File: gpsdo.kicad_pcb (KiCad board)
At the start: 2 copper layers, 124 parts, among them U1 LM2937IMP-5.0, U10 MC12080, U11 MSA-0385, U12 MSA-0385, U13 MSA-0385, U14 MSA-0385, U15 MSA-0385, U16 MSA-0385, U17 MSA-0385, U18 MSA-0385, U19 MSA-0385, U2 LM2937IMP-8.0, U20 MSA-0385, U21 MSA-0385, U3 SN74HC244, U4 TPS79333-EP, U5 ADP7142ARDZ-5.0-R7, U6 DAC8571IDGKR, U7 LEA-M8F, U8 CVSS-945, U9 SN74HC244

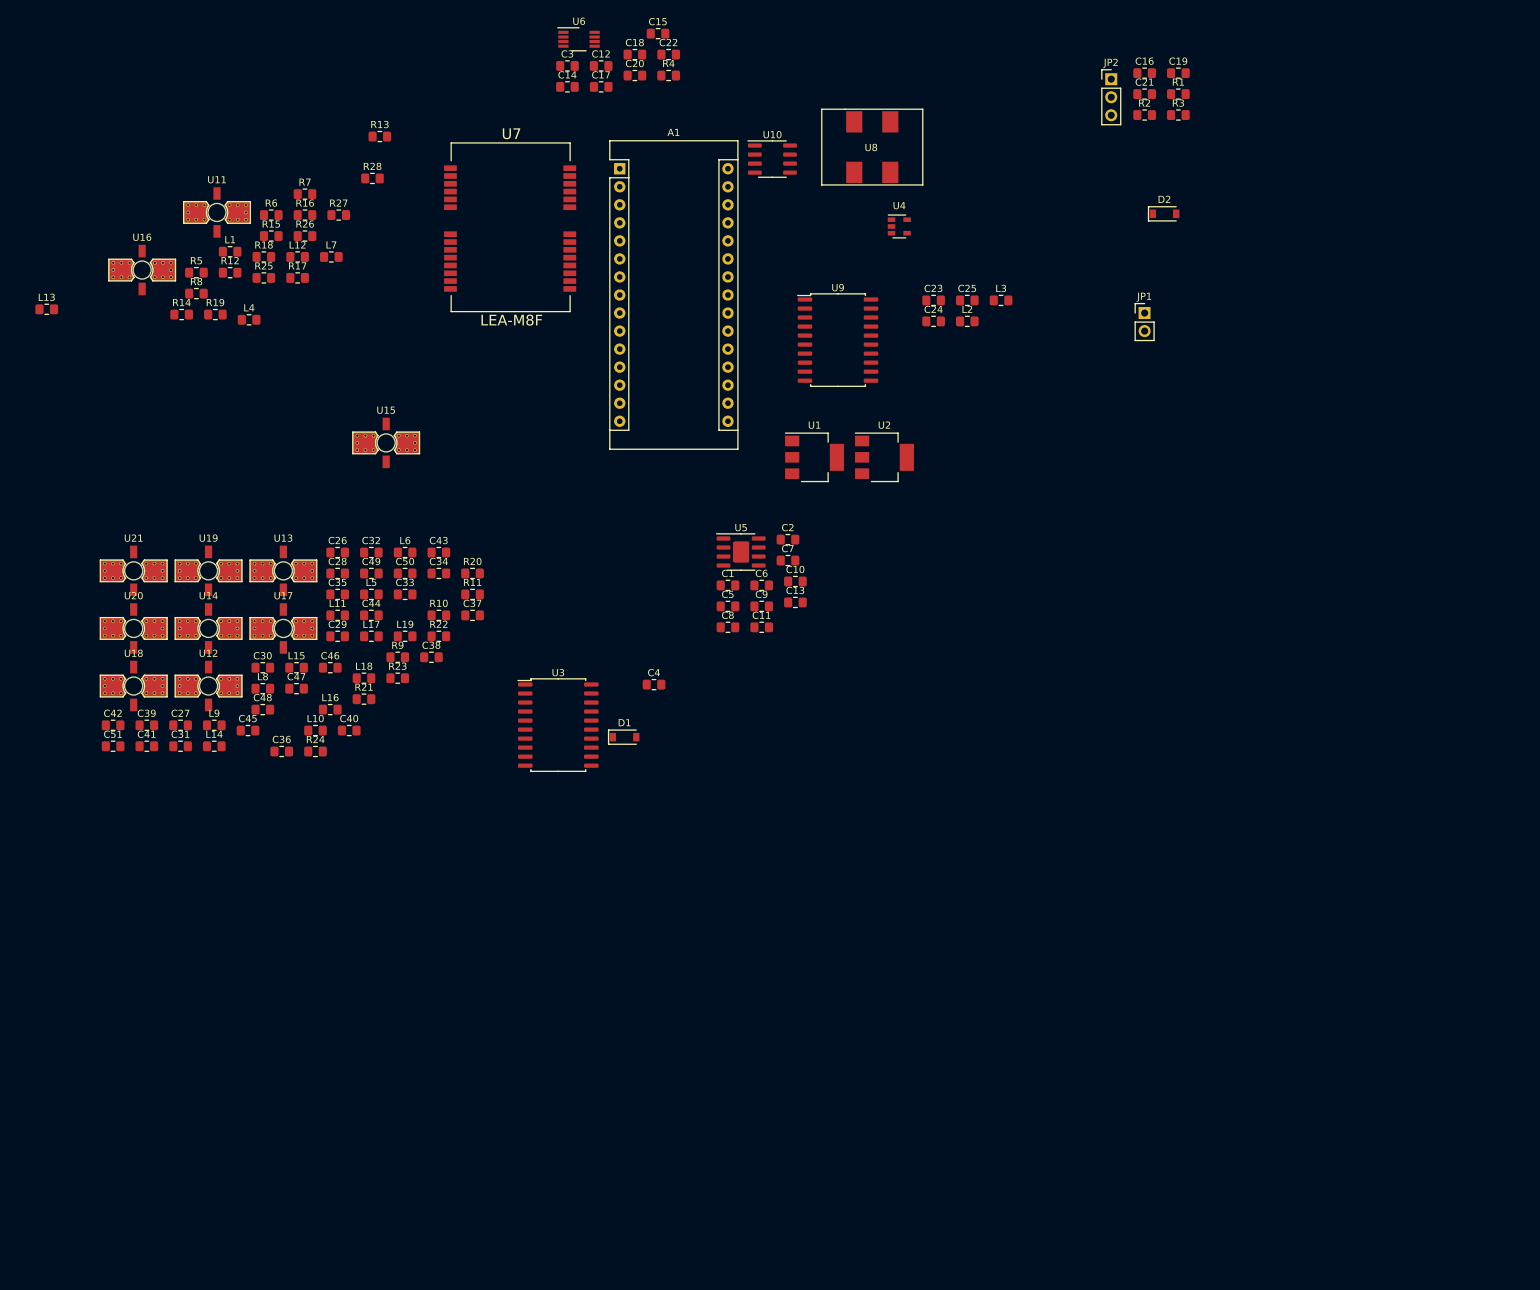
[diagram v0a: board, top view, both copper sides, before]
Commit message: Implemented fixes following Frederic's review
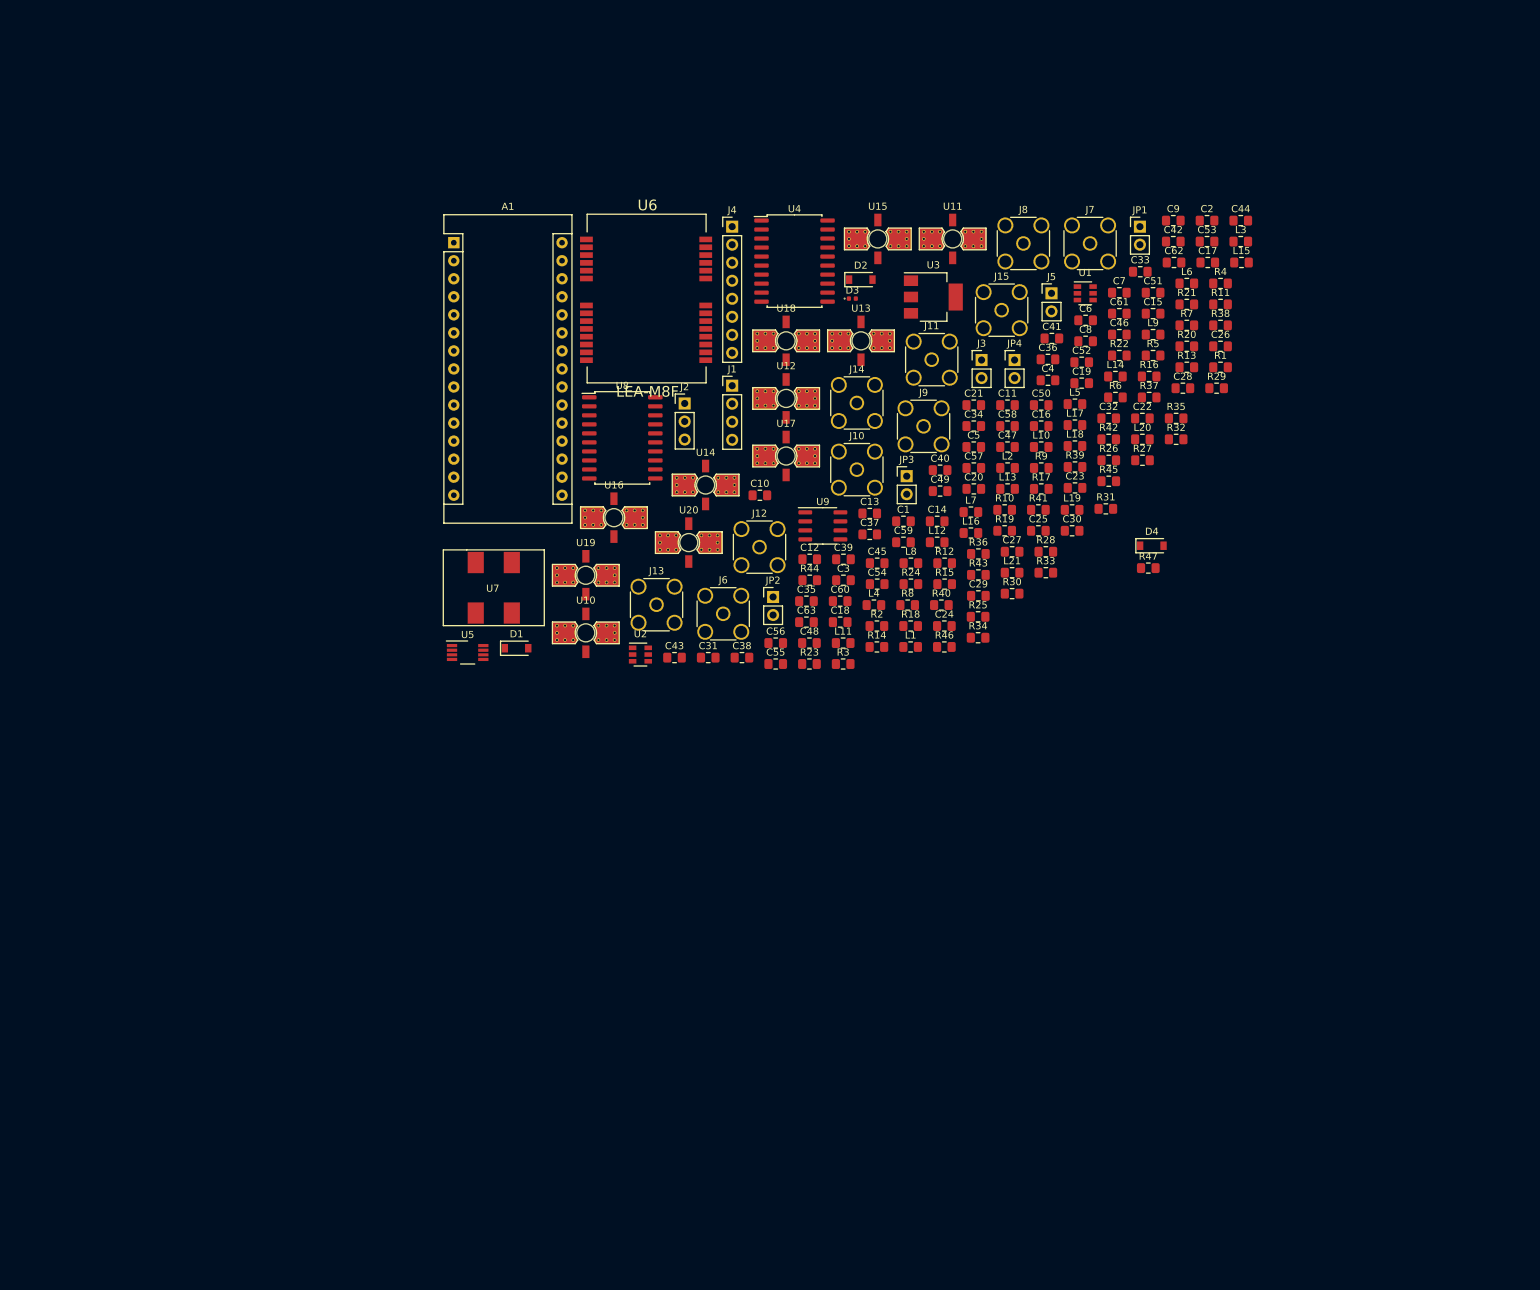
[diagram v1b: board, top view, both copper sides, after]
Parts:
- removed U21: MSA-0385, yo6ssw:PL262
- added C52: 0.1uF, Capacitor_SMD:C_0805_2012Metric_Pad1.15x1.40mm_HandSolder, F.Cu at (166.4, 73.0)
- added C53: 0.1uF, Capacitor_SMD:C_0805_2012Metric_Pad1.15x1.40mm_HandSolder, F.Cu at (184.0, 56.0)
- added C54: 0.1uF, Capacitor_SMD:C_0805_2012Metric_Pad1.15x1.40mm_HandSolder, F.Cu at (137.6, 104.2)
- added C55: 0.1uF, Capacitor_SMD:C_0805_2012Metric_Pad1.15x1.40mm_HandSolder, F.Cu at (123.3, 115.5)
- added C56: 0.1uF, Capacitor_SMD:C_0805_2012Metric_Pad1.15x1.40mm_HandSolder, F.Cu at (123.3, 112.5)
- added C57: 0.1uF, Capacitor_SMD:C_0805_2012Metric_Pad1.15x1.40mm_HandSolder, F.Cu at (151.2, 87.9)
- added C58: 0.1uF, Capacitor_SMD:C_0805_2012Metric_Pad1.15x1.40mm_HandSolder, F.Cu at (155.9, 82.0)
- added C59: 0.1uF, Capacitor_SMD:C_0805_2012Metric_Pad1.15x1.40mm_HandSolder, F.Cu at (141.3, 98.3)
- added C60: 0.1uF, Capacitor_SMD:C_0805_2012Metric_Pad1.15x1.40mm_HandSolder, F.Cu at (132.4, 106.6)
- added C61: 0.1uF, Capacitor_SMD:C_0805_2012Metric_Pad1.15x1.40mm_HandSolder, F.Cu at (171.7, 66.1)
- added C62: 0.1uF, Capacitor_SMD:C_0805_2012Metric_Pad1.15x1.40mm_HandSolder, F.Cu at (179.4, 58.9)
- added C63: 0.1uF, Capacitor_SMD:C_0805_2012Metric_Pad1.15x1.40mm_HandSolder, F.Cu at (127.6, 109.6)
- added D3: ESD9R3.3ST5G, Diode_SMD:D_0402_1005Metric, F.Cu at (134.1, 64.0)
- added D4: 1N4148W, Diode_SMD:D_SOD-123, F.Cu at (176.3, 98.8)
- added J1: OLED, Connector_PinHeader_2.54mm:PinHeader_1x04_P2.54mm_Vertical, F.Cu at (117.2, 76.3)
- added J10: 10MHZ_OUT, Connector_Coaxial:SMA_Amphenol_132134_Vertical, F.Cu at (134.7, 88.1)
- added J11: 100MHZ_OUT, Connector_Coaxial:SMA_Amphenol_132134_Vertical, F.Cu at (145.3, 72.6)
- added J12: 10MHZ_OUT, Connector_Coaxial:SMA_Amphenol_132134_Vertical, F.Cu at (121.0, 99.0)
- added J13: 10MHZ_OUT, Connector_Coaxial:SMA_Amphenol_132134_Vertical, F.Cu at (106.5, 107.1)
- added J14: 10MHZ_OUT, Connector_Coaxial:SMA_Amphenol_132134_Vertical, F.Cu at (134.7, 78.7)
- added J15: 10MHZ_OUT, Connector_Coaxial:SMA_Amphenol_132134_Vertical, F.Cu at (155.1, 65.6)
- added J2: ARDUINO_UART, Connector_PinHeader_2.54mm:PinHeader_1x03_P2.54mm_Vertical, F.Cu at (110.5, 78.8)
- added J3: VOLTMETER, Connector_PinHeader_2.54mm:PinHeader_1x02_P2.54mm_Vertical, F.Cu at (152.3, 72.7)
- added J4: ARDUINO_EXTRA_PINS, Connector_PinHeader_2.54mm:PinHeader_1x08_P2.54mm_Vertical, F.Cu at (117.2, 53.9)
- added J5: POWER_IN, Connector_PinHeader_2.54mm:PinHeader_1x02_P2.54mm_Vertical, F.Cu at (162.1, 63.3)
- added J6: GPS_ANT, Connector_Coaxial:SMA_Amphenol_132134_Vertical, F.Cu at (115.9, 108.4)
- added J7: 10MHZ_OUT, Connector_Coaxial:SMA_Amphenol_132134_Vertical, F.Cu at (167.6, 56.2)
- added J8: 10MHZ_OUT, Connector_Coaxial:SMA_Amphenol_132134_Vertical, F.Cu at (158.2, 56.2)
- added J9: 10MHZ_OUT, Connector_Coaxial:SMA_Amphenol_132134_Vertical, F.Cu at (144.1, 82.0)
- added JP3: JP_BUF_1_OUT, Connector_PinHeader_2.54mm:PinHeader_1x02_P2.54mm_Vertical, F.Cu at (141.8, 89.0)
- added JP4: JP_BUF_2_OUT, Connector_PinHeader_2.54mm:PinHeader_1x02_P2.54mm_Vertical, F.Cu at (156.9, 72.7)
- added L20: 1uH, Inductor_SMD:L_0805_2012Metric_Pad1.15x1.40mm_HandSolder, F.Cu at (174.9, 83.8)
- added L21: 1uH, Inductor_SMD:L_0805_2012Metric_Pad1.15x1.40mm_HandSolder, F.Cu at (156.6, 102.6)
- added R29: 86.6Ω 1%, Resistor_SMD:R_0805_2012Metric_Pad1.15x1.40mm_HandSolder, F.Cu at (185.4, 76.6)
- added R30: 86.6Ω 1%, Resistor_SMD:R_0805_2012Metric_Pad1.15x1.40mm_HandSolder, F.Cu at (156.6, 105.6)
- added R31: 86.6Ω 1%, Resistor_SMD:R_0805_2012Metric_Pad1.15x1.40mm_HandSolder, F.Cu at (169.8, 93.6)
- added R32: 30Ω, Resistor_SMD:R_0805_2012Metric_Pad1.15x1.40mm_HandSolder, F.Cu at (179.7, 83.8)
- added R33: 30Ω, Resistor_SMD:R_0805_2012Metric_Pad1.15x1.40mm_HandSolder, F.Cu at (161.3, 102.6)
- added R34: 30Ω, Resistor_SMD:R_0805_2012Metric_Pad1.15x1.40mm_HandSolder, F.Cu at (151.8, 111.8)
- added R35: 30Ω, Resistor_SMD:R_0805_2012Metric_Pad1.15x1.40mm_HandSolder, F.Cu at (179.7, 80.9)
- added R36: 30Ω, Resistor_SMD:R_0805_2012Metric_Pad1.15x1.40mm_HandSolder, F.Cu at (151.8, 100.0)
- added R37: 30Ω, Resistor_SMD:R_0805_2012Metric_Pad1.15x1.40mm_HandSolder, F.Cu at (175.9, 77.9)
- added R38: 86.6Ω 1%, Resistor_SMD:R_0805_2012Metric_Pad1.15x1.40mm_HandSolder, F.Cu at (185.9, 67.8)
- added R39: 86.6Ω 1%, Resistor_SMD:R_0805_2012Metric_Pad1.15x1.40mm_HandSolder, F.Cu at (165.5, 87.7)
- added R40: 86.6Ω 1%, Resistor_SMD:R_0805_2012Metric_Pad1.15x1.40mm_HandSolder, F.Cu at (146.6, 107.2)
- added R41: 86.6Ω 1%, Resistor_SMD:R_0805_2012Metric_Pad1.15x1.40mm_HandSolder, F.Cu at (160.3, 93.8)
- added R42: 86.6Ω 1%, Resistor_SMD:R_0805_2012Metric_Pad1.15x1.40mm_HandSolder, F.Cu at (170.2, 83.8)
- added R43: 30Ω, Resistor_SMD:R_0805_2012Metric_Pad1.15x1.40mm_HandSolder, F.Cu at (151.8, 102.9)
- added R44: 30Ω, Resistor_SMD:R_0805_2012Metric_Pad1.15x1.40mm_HandSolder, F.Cu at (128.1, 103.7)
- added R45: 30Ω, Resistor_SMD:R_0805_2012Metric_Pad1.15x1.40mm_HandSolder, F.Cu at (170.2, 89.7)
- added R46: 30Ω, Resistor_SMD:R_0805_2012Metric_Pad1.15x1.40mm_HandSolder, F.Cu at (147.1, 113.1)
- added R47: 100KΩ, Resistor_SMD:R_0805_2012Metric_Pad1.15x1.40mm_HandSolder, F.Cu at (175.8, 102.0)
- C10: value 3.3uF/6.3V -> 15pF
- C11: value 0.01uF -> 0.1uF
- C12, C19, C2, C20, C3, C4: value 0.1uF -> 1uF
- C13: value 2.2uF/10V -> 1uF
- C14: value 0.1uF -> 2.2uF/6.3V
- C15: value 0.1uF -> 2.2uF/10V
- C17, C18: value 1nF -> 0.1uF
- C22: value CL -> 0.1uF
- C23, C25, C39: value 10p -> 0.1uF
- C24: value 100p -> 0.1uF
- C27, C28: value 0.1uF -> 1nF
- C29: value 0.1uF -> 100pF
- C31, C35, C36: value 0.1uF -> 443.2pF
- C33: value 10p -> CL
- C34: value 100p -> 519.8pF
- C44, C50, C51: value 0.1uF -> 44.32pF
- C45: value 0.1uF -> 51.98pF
- C5: value 10uF/10V/ESR=2 -> 0.1uF
- C6: value 10uF/16V/ESR=2 -> 0.1uF
- C7: value 0.1uF -> 0.01uF
- C8: value 2.2uF/20V -> 0.01uF
- C9: value 0.01uF -> 15pF
- D2: value ANT_PROTECTION -> 1N4148W
- JP1: value JMP_DAC_VOLTAGE -> JP_BUF_1_IN
- JP2: value GPS_ANT_TYPE -> JP_BUF_2_IN; footprint Connector_PinHeader_2.54mm:PinHeader_1x03_P2.54mm_Vertical -> Connector_PinHeader_2.54mm:PinHeader_1x02_P2.54mm_Vertical
- L1, L2, L3, L4: value 2.2uH -> 10uH
- L11, L14: value 2.2uH -> 1uH
- L13, L8: value 1uH -> 139.1nH
- L16: value 1uH -> 63.42nH
- L5, L6: value 2.2uH -> 1.391uH
- L7: value 1uH -> 0.634uH
- R1: value 16.7Ω -> 100KΩ
- R10, R9: value 86.6Ω 1% -> 30KΩ
- R11, R12: value 86.6Ω 1% -> TBD
- R13: value 86.6Ω 1% -> 10K
- R14: value 30Ω -> 10K
- R15, R16: value 30Ω -> 100KΩ
- R17: value 30Ω -> 16.7Ω
- R18, R19, R25: value 30Ω -> 16.7Ω 1%
- R2: value 16.7Ω 1% -> 100KΩ
- R20: value 86.6Ω 1% -> 820Ω
- R21: value 86.6Ω 1% -> 220Ω
- R22: value 86.6Ω 1% -> 68Ω
- R23: value 86.6Ω 1% -> 16.7Ω
- R24: value 86.6Ω 1% -> 16.7Ω 1%
- R26, R27, R28: value 30Ω -> 86.6Ω 1%
- R3: value 16.7Ω 1% -> 18KΩ
- R4: value RL -> 33KΩ
- R5: value 16.7Ω -> 1.3KΩ
- R6: value 16.7Ω 1% -> 240Ω
- R7: value 16.7Ω 1% -> 56KΩ
- R8: value 86.6Ω 1% -> 93KΩ
- U1: value LM2937IMP-5.0 -> TPS79301-EP; footprint Package_TO_SOT_SMD:SOT-223-3_TabPin2 -> Package_TO_SOT_SMD:SOT-23-6
- U10: value MC12080 -> MSA-0385; footprint Package_SO:SOIC-8_3.9x4.9mm_P1.27mm -> yo6ssw:PL262
- U2: value LM2937IMP-8.0 -> TPS79301-EP; footprint Package_TO_SOT_SMD:SOT-223-3_TabPin2 -> Package_TO_SOT_SMD:SOT-23-6
- U3: value SN74HC244 -> LM317DCYR; footprint Package_SO:SOIC-20W_7.5x12.8mm_P1.27mm -> Package_TO_SOT_SMD:SOT-223
- U4: value TPS79333-EP -> SN74HC244; footprint Package_TO_SOT_SMD:SOT-23-5 -> Package_SO:SOIC-20W_7.5x12.8mm_P1.27mm
- U5: value ADP7142ARDZ-5.0-R7 -> DAC8571IDGKR; footprint Package_SO:SOIC-8-1EP_3.9x4.9mm_P1.27mm_EP2.29x3mm -> Package_SO:VSSOP-8_3.0x3.0mm_P0.65mm
- U6: value DAC8571IDGKR -> LEA-M8F; footprint Package_SO:VSSOP-8_3.0x3.0mm_P0.65mm -> yo6ssw:LEA-8MF
- U7: value LEA-M8F -> CVSS-945; footprint yo6ssw:LEA-8MF -> yo6ssw:CVSS-945
- U8: value CVSS-945 -> SN74HC244; footprint yo6ssw:CVSS-945 -> Package_SO:SOIC-20W_7.5x12.8mm_P1.27mm
- U9: value SN74HC244 -> MC12080; footprint Package_SO:SOIC-20W_7.5x12.8mm_P1.27mm -> Package_SO:SOIC-8_3.9x4.9mm_P1.27mm
- moved C42 164.1 mm to (179.3, 56.0)
- moved C51 159.8 mm to (176.4, 63.2)
- moved L15 144.8 mm to (188.9, 58.9)
- moved L9 143.2 mm to (176.4, 69.1)
- moved C41 139.8 mm to (162.2, 69.6)
- moved L13 137.6 mm to (156.0, 90.8)
- moved L14 137.2 mm to (171.1, 75.0)
- moved R5 135.2 mm to (176.4, 72.0)
- moved C44 134.5 mm to (188.8, 53.0)
- moved R21 128.5 mm to (181.2, 64.8)
- moved C26 127.7 mm to (185.9, 70.7)
- moved R7 125.5 mm to (181.2, 67.8)
- moved C28 121.9 mm to (180.6, 76.6)
- moved R6 121.6 mm to (171.1, 77.9)
- moved C36 121.2 mm to (161.6, 72.6)
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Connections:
- A1 pad 1: (no net) -> ARDUINO_UART_TX
- A1 pad 10: (no net) -> ARDUINO_D7
- A1 pad 12: (no net) -> VOLTMETER
- A1 pad 13: ARDUINO_RX -> A2G_RX
- A1 pad 14: ARDUINO_TX -> A2G_TX
- A1 pad 2: (no net) -> ARDUINO_UART_RX
- A1 pad 23: (no net) -> ARDUINO_SDA
- A1 pad 24: (no net) -> ARDUINO_SCL
- A1 pad 27: (no net) -> ARDUINO_5V
- A1 pad 30: V_ARDUINO -> Net-(A1-Pad30)
- A1 pad 5: (no net) -> ARDUINO_D2
- A1 pad 6: (no net) -> ARDUINO_D3
- A1 pad 7: (no net) -> ARDUINO_D4
- A1 pad 8: (no net) -> ARDUINO_D5
- A1 pad 9: (no net) -> ARDUINO_D6
- C1 pad 1: GND -> 10MHZ
- C1 pad 2: Vin -> Net-(C1-Pad2)
- C10 pad 1: V_GPS -> V_VCXO
- C10 pad 2: GND -> Net-(C10-Pad2)
- C11 pad 2: Net-(C11-Pad2) -> V_GPS
- C12 pad 2: V_GPS -> Net-(C12-Pad2)
- C13 pad 1: V_VCXO -> GND
- C13 pad 2: GND -> V_MMIC
- C14 pad 2: Net-(C14-Pad2) -> V_GPS
- C16 pad 1: 100MHZ_IN -> GND
- C16 pad 2: Net-(C16-Pad2) -> V_GPS
- C17 pad 1: Net-(C17-Pad1) -> GND
- C19 pad 2: V_ARDUINO -> Net-(C19-Pad2)
- C2 pad 2: Vin -> V_IN
- C20 pad 2: V_ARDUINO -> Net-(C20-Pad2)
- C21 pad 1: Net-(C21-Pad1) -> 10MHZ
- C21 pad 2: 100MHZ_IN -> Net-(C21-Pad2)
- C22 pad 2: 10MHZ_IN -> V_VCXO
- C24 pad 1: Net-(C24-Pad1) -> 100MHZ_FILTER
- C24 pad 2: GND -> Net-(C24-Pad2)
- C25 pad 1: Net-(C25-Pad1) -> GND
- C25 pad 2: GND -> V_VCXO
- C26 pad 1: Net-(C26-Pad1) -> GND
- C27 pad 1: /A1_IN -> Net-(C27-Pad1)
- C28 pad 1: /A3_IN -> GND
- C29 pad 1: /A5_IN -> GND
- C29 pad 2: Net-(C29-Pad2) -> V_VCXO
- C3 pad 2: V_ARDUINO -> V_IN
- C30 pad 1: /A7_IN -> GND
- C30 pad 2: Net-(C30-Pad2) -> V_VCXO
- C31 pad 1: Net-(C31-Pad1) -> GND
- C31 pad 2: Net-(C31-Pad2) -> 10MHZ_FILTER
- C33 pad 2: Net-(C33-Pad2) -> 10MHZ
- C35 pad 2: (no net) -> GND
- C36 pad 2: (no net) -> GND
- C37 pad 1: Net-(C37-Pad1) -> Net-(C36-Pad1)
- C37 pad 2: (no net) -> Net-(C37-Pad2)
- C38 pad 1: Net-(C38-Pad1) -> /A1_IN
- C38 pad 2: (no net) -> Net-(C38-Pad2)
- C39 pad 1: Net-(C39-Pad1) -> /A3_IN
- C39 pad 2: GND -> Net-(C39-Pad2)
- C4 pad 2: V_GPS -> V_IN
- C40 pad 1: Net-(C40-Pad1) -> /A5_IN
- C41 pad 1: Net-(C41-Pad1) -> /A7_IN
- C43 pad 1: /A2_IN -> Net-(C43-Pad1)
- C44 pad 1: /A4_IN -> 100MHZ_FILTER
- C44 pad 2: Net-(C44-Pad2) -> GND
- C45 pad 1: /A6_IN -> Net-(C45-Pad1)
- C45 pad 2: Net-(C45-Pad2) -> GND
- C46 pad 1: /A8_IN -> Net-(C46-Pad1)
- C46 pad 2: Net-(C46-Pad2) -> /A1_OUT
- C47 pad 2: (no net) -> /A3_OUT
- C48 pad 2: (no net) -> /A5_OUT
- C49 pad 2: (no net) -> /A7_OUT
- C5 pad 1: V_ARDUINO -> GND
- C5 pad 2: GND -> V_MMIC
- C50 pad 2: (no net) -> GND
- C51 pad 2: (no net) -> GND
- C6 pad 1: V_MMIC -> GND
- C6 pad 2: GND -> Net-(A1-Pad30)
- C7 pad 2: Vin -> Net-(C7-Pad2)
- C8 pad 1: Vin -> GND
- C8 pad 2: GND -> Net-(C8-Pad2)
- C9 pad 1: GND -> V_GPS
- D1 pad 1: Net-(C14-Pad2) -> V_IN
- D1 pad 2: V_VCXO -> V_MMIC
- D2 pad 1: GPS_ANTENNA -> V_MMIC
- D2 pad 2: GND -> Net-(C12-Pad2)
- JP1 pad 1: Net-(C14-Pad2) -> Net-(JP1-Pad1)
- JP1 pad 2: V_VCXO -> Net-(C21-Pad2)
- JP2 pad 1: GND -> Net-(JP2-Pad1)
- JP2 pad 2: Net-(JP2-Pad2) -> Net-(C21-Pad2)
- L1 pad 1: 100MHZ_IN -> V_MMIC
- L1 pad 2: Net-(C23-Pad2) -> Net-(A1-Pad30)
- L10 pad 2: Net-(C38-Pad1) -> Net-(C47-Pad1)
- L11 pad 1: Net-(C34-Pad1) -> Net-(L11-Pad1)
- L11 pad 2: Net-(C39-Pad1) -> Net-(C48-Pad1)
- L12 pad 2: Net-(C40-Pad1) -> Net-(C49-Pad1)
- L13 pad 1: Net-(L13-Pad1) -> Net-(C45-Pad1)
- L13 pad 2: Net-(C41-Pad1) -> Net-(C50-Pad1)
- L14 pad 1: Net-(C39-Pad1) -> Net-(L14-Pad1)
- L14 pad 2: Net-(C42-Pad1) -> Net-(C52-Pad1)
- L15 pad 2: Net-(C51-Pad1) -> Net-(C53-Pad1)
- L16 pad 1: Net-(L16-Pad1) -> Net-(C50-Pad1)
- L16 pad 2: Net-(C47-Pad1) -> Net-(C51-Pad1)
- L17 pad 2: Net-(C48-Pad1) -> Net-(C63-Pad1)
- L18 pad 2: Net-(C49-Pad1) -> Net-(C59-Pad1)
- L19 pad 2: Net-(C50-Pad1) -> Net-(C60-Pad1)
- L2 pad 1: Net-(C23-Pad2) -> V_GPS
- L2 pad 2: Net-(C24-Pad1) -> Net-(C17-Pad2)
- L3 pad 1: Net-(C24-Pad1) -> V_VCXO
- L3 pad 2: Net-(C25-Pad1) -> Net-(C23-Pad2)
- L4 pad 1: Net-(C25-Pad1) -> V_VCXO
- L4 pad 2: Net-(C26-Pad1) -> Net-(C26-Pad2)
- L5 pad 1: (no net) -> 10MHZ_FILTER
- L5 pad 2: Net-(C33-Pad2) -> Net-(C34-Pad1)
- L6 pad 1: Net-(C33-Pad2) -> Net-(C34-Pad1)
- L6 pad 2: Net-(C34-Pad1) -> Net-(C35-Pad1)
- L7 pad 1: Net-(L7-Pad1) -> Net-(C35-Pad1)
- L7 pad 2: Net-(C35-Pad1) -> Net-(C36-Pad1)
- L8 pad 1: Net-(L8-Pad1) -> 100MHZ_FILTER
- L8 pad 2: Net-(C36-Pad1) -> Net-(C45-Pad1)
- L9 pad 2: Net-(C37-Pad1) -> Net-(C46-Pad1)
- R1 pad 1: Net-(R1-Pad1) -> Net-(C1-Pad2)
- R1 pad 2: Net-(R1-Pad2) -> V_GPS
- R10 pad 1: V_MMIC -> V_VCXO
- R10 pad 2: Net-(L9-Pad1) -> GND
- R11 pad 1: V_MMIC -> Net-(C18-Pad2)
- R11 pad 2: Net-(L10-Pad1) -> V_VCXO
- R12 pad 1: V_MMIC -> GND
- R12 pad 2: Net-(L12-Pad1) -> Net-(C18-Pad2)
- R13 pad 1: V_MMIC -> Net-(C19-Pad2)
- R13 pad 2: Net-(L13-Pad1) -> Net-(R13-Pad2)
- R14 pad 1: Net-(R14-Pad1) -> Net-(C20-Pad2)
- R14 pad 2: Net-(C40-Pad2) -> Net-(C19-Pad2)
- R15 pad 1: Net-(R15-Pad1) -> Net-(C21-Pad2)
- R15 pad 2: Net-(C41-Pad2) -> V_ARDUINO
- R16 pad 1: /A1_IN -> GND
- R16 pad 2: Net-(R14-Pad1) -> (no net)
- R17 pad 1: /A5_IN -> Net-(R17-Pad1)
- R17 pad 2: Net-(R15-Pad1) -> Net-(R17-Pad2)
- R18 pad 1: /A2_IN -> Net-(C24-Pad2)
- R18 pad 2: Net-(R14-Pad1) -> Net-(R17-Pad1)
- R19 pad 1: /A6_IN -> Net-(C27-Pad1)
- R19 pad 2: Net-(R15-Pad1) -> Net-(R17-Pad1)
- R2 pad 1: Net-(C16-Pad2) -> Net-(C1-Pad2)
- R2 pad 2: Net-(R1-Pad1) -> GND
- R20 pad 1: V_MMIC -> 10MHZ
- R20 pad 2: Net-(L15-Pad1) -> GND
- R21 pad 1: V_MMIC -> 10MHZ_FILTER
- R21 pad 2: Net-(L16-Pad1) -> Net-(C32-Pad2)
- R22 pad 1: V_MMIC -> GND
- R22 pad 2: Net-(L17-Pad1) -> 10MHZ_FILTER
- R23 pad 1: V_MMIC -> Net-(R23-Pad1)
- R23 pad 2: Net-(L18-Pad1) -> Net-(C37-Pad2)
- R24 pad 1: V_MMIC -> Net-(C42-Pad1)
- R24 pad 2: Net-(L19-Pad1) -> Net-(R23-Pad1)
- R25 pad 1: /A3_IN -> Net-(C43-Pad1)
- R25 pad 2: Net-(R14-Pad1) -> Net-(R23-Pad1)
- R26 pad 1: /A7_IN -> V_MMIC
- R26 pad 2: Net-(R15-Pad1) -> Net-(L9-Pad1)
- R27 pad 1: /A4_IN -> V_MMIC
- R27 pad 2: Net-(R14-Pad1) -> Net-(L10-Pad1)
- R28 pad 1: /A8_IN -> V_MMIC
- R28 pad 2: Net-(R15-Pad1) -> Net-(L11-Pad1)
- R3 pad 1: Net-(C17-Pad1) -> Net-(R3-Pad1)
- R3 pad 2: Net-(R1-Pad1) -> A2G_TX
- R4 pad 1: 10MHZ_IN -> Net-(R3-Pad1)
- R5 pad 1: Net-(R5-Pad1) -> Net-(C12-Pad2)
- R5 pad 2: Net-(C26-Pad2) -> GND
- R6 pad 1: Net-(C31-Pad1) -> V_MMIC
- R6 pad 2: Net-(R5-Pad1) -> Net-(C12-Pad2)
- R7 pad 1: Net-(C32-Pad1) -> Net-(C9-Pad2)
- R7 pad 2: Net-(R5-Pad1) -> V_GPS
- R8 pad 1: V_MMIC -> Net-(C10-Pad2)
- R8 pad 2: Net-(L7-Pad1) -> V_VCXO
- R9 pad 1: V_MMIC -> V_GPS
- R9 pad 2: Net-(L8-Pad1) -> GND
- U1 pad 1: Vin -> V_IN
- U1 pad 3: V_ARDUINO -> V_IN
- U10 pad 1: Net-(C17-Pad2) -> Net-(C38-Pad2)
- U10 pad 2: V_ARDUINO -> GND
- U10 pad 3: V_ARDUINO -> Net-(C46-Pad1)
- U10 pad 4: 10MHZ_IN -> GND
- U11 pad 1: Net-(C27-Pad2) -> Net-(C39-Pad2)
- U11 pad 3: Net-(C35-Pad1) -> Net-(C47-Pad1)
- U12 pad 1: Net-(C28-Pad2) -> Net-(C40-Pad2)
- U12 pad 3: Net-(C36-Pad1) -> Net-(C48-Pad1)
- U13 pad 1: Net-(C29-Pad2) -> Net-(C41-Pad2)
- U13 pad 3: Net-(C37-Pad1) -> Net-(C49-Pad1)
- U14 pad 1: Net-(C30-Pad2) -> Net-(C42-Pad2)
- U14 pad 3: Net-(C38-Pad1) -> Net-(C52-Pad1)
- U15 pad 1: Net-(C31-Pad2) -> Net-(C43-Pad2)
- U15 pad 3: Net-(C40-Pad1) -> Net-(C53-Pad1)
- U16 pad 1: Net-(C32-Pad2) -> Net-(C54-Pad2)
- U16 pad 3: Net-(C41-Pad1) -> Net-(C63-Pad1)
- U17 pad 1: Net-(C42-Pad2) -> Net-(C55-Pad2)
- U17 pad 3: Net-(C51-Pad1) -> Net-(C59-Pad1)
- U18 pad 1: Net-(C43-Pad2) -> Net-(C56-Pad2)
- U18 pad 3: Net-(C47-Pad1) -> Net-(C60-Pad1)
- U19 pad 1: Net-(C44-Pad2) -> Net-(C57-Pad2)
- U19 pad 3: Net-(C48-Pad1) -> Net-(C61-Pad1)
- U2 pad 1: Vin -> V_IN
- U2 pad 3: V_MMIC -> V_IN
- U20 pad 1: Net-(C45-Pad2) -> Net-(C58-Pad2)
- U20 pad 3: Net-(C49-Pad1) -> Net-(C62-Pad1)
- U3 pad 1: GND -> Net-(C12-Pad2)
- U3 pad 2: ARDUINO_TX -> V_MMIC
- U3 pad 3: (no net) -> V_IN
- U3 pad 4: GPS_TX -> V_MMIC
- U4 pad 1: Vin -> GND
- U4 pad 2: GND -> Net-(R3-Pad1)
- U4 pad 3: Vin -> (no net)
- U4 pad 4: Net-(C9-Pad2) -> GPS_TX
- U4 pad 5: V_GPS -> (no net)
- U5 pad 1: V_VCXO -> Net-(C18-Pad2)
- U5 pad 2: V_VCXO -> Net-(C18-Pad2)
- U5 pad 3: V_VCXO -> Net-(R13-Pad2)
- U5 pad 4: GND -> Net-(R13-Pad2)
- U5 pad 5: Vin -> GND
- U5 pad 6: Net-(C11-Pad2) -> DAC_SCL
- U5 pad 7: Vin -> DAC_SDA
- U5 pad 8: Vin -> GND
- U6 pad 1: Net-(C14-Pad2) -> (no net)
- U6 pad 2: Net-(C14-Pad2) -> (no net)
- U6 pad 3: Net-(U6-Pad3) -> GPS_TX
- U6 pad 4: Net-(U6-Pad3) -> GPS_RX
- U6 pad 5: GND -> (no net)
- U6 pad 6: DAC_SCL -> Net-(C17-Pad2)
- U6 pad 7: DAC_SDA -> GND
- U6 pad 8: GND -> (no net)
- U7 pad 1: (no net) -> Net-(C20-Pad2)
- U7 pad 2: (no net) -> GND
- U7 pad 3: GPS_TX -> Net-(R17-Pad2)
- U7 pad 4: GPS_RX -> Net-(C23-Pad2)
- U8 pad 1: Net-(U6-Pad3) -> GND
- U8 pad 2: GND -> Net-(C21-Pad2)
- U8 pad 3: Net-(R1-Pad2) -> (no net)
- U8 pad 4: V_VCXO -> Net-(JP1-Pad1)
- U9 pad 1: GND -> Net-(C27-Pad2)
- U9 pad 2: 10MHZ_IN -> V_VCXO
- U9 pad 3: (no net) -> V_VCXO
- U9 pad 4: (no net) -> 10MHZ
- U9 pad 5: (no net) -> GND
- U9 pad 6: (no net) -> V_VCXO
- U9 pad 7: (no net) -> V_VCXO
- U9 pad 8: (no net) -> Net-(C28-Pad2)
